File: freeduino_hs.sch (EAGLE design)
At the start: 46 parts, among them J1 DC-005, Q1 16 MHz, Q2 12 MHz, T1 FDN340P, U1 CH340G, U2 LM393D, U3 ATMEGA328P-PU, U4 REG1117, U5 REG1117, X1 MINI-USB-32005-201

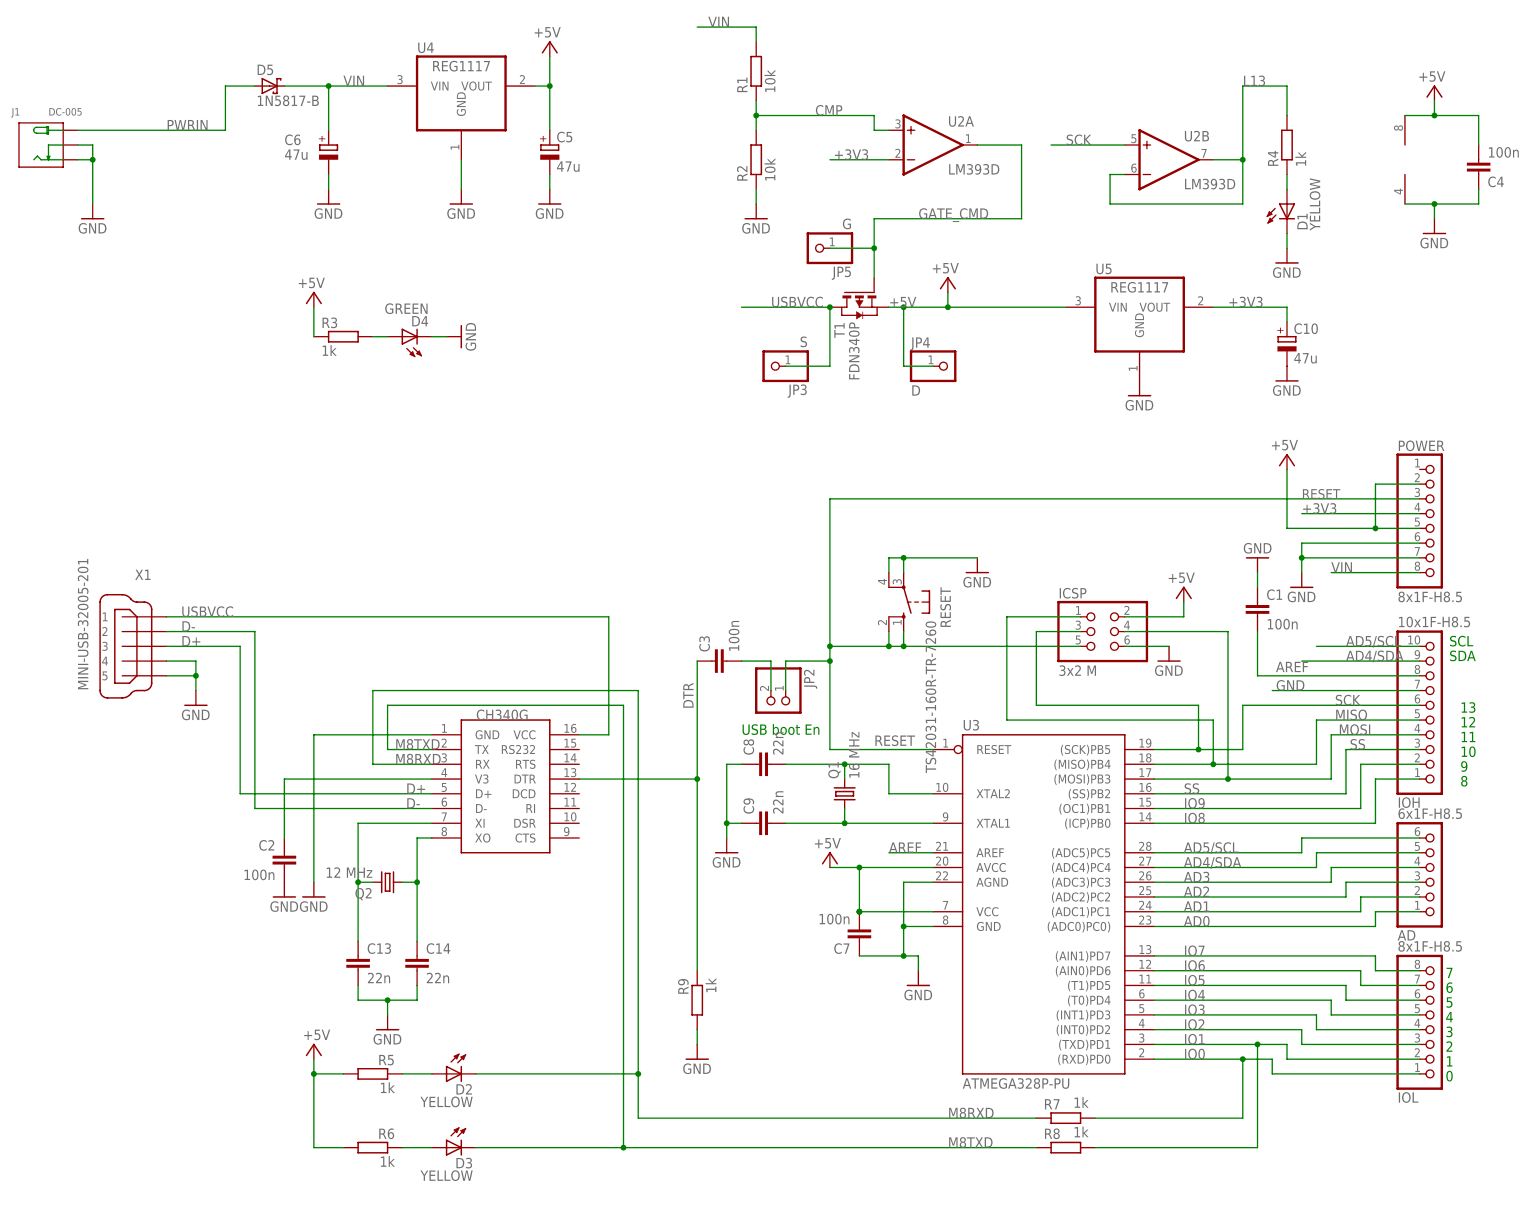
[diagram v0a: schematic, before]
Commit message: Fix TX-RX routing
Move ISP connector
Add reset pull-up resistor
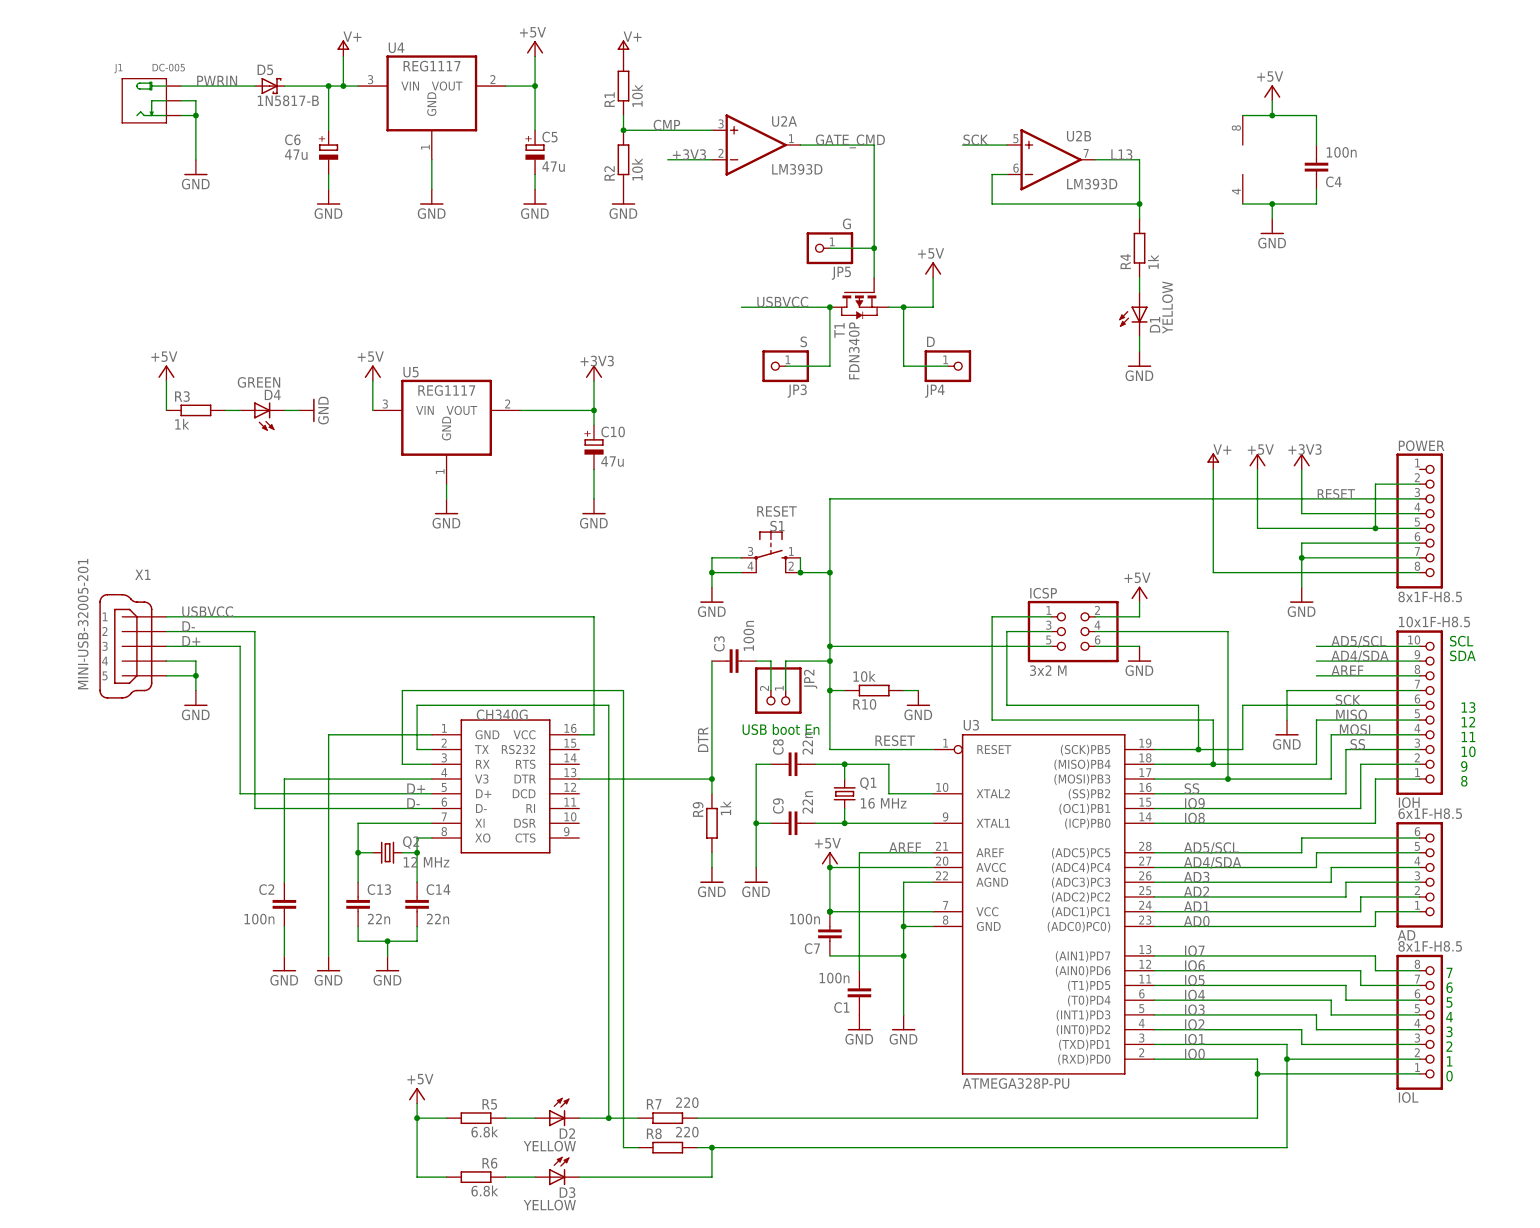
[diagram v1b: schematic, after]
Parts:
- removed RESET: TS42031-160R-TR-7260, switch-omron:10-XX
- added R10: 10k, resistor:R-EU_0204/7
- added S1: RESET, switch-omron:10-XX
- R5, R6: value 1k -> 6.8k
- R7, R8: value 1k -> 220
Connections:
- net VIN renamed V+
- removed net M8TXD: D3.C, R8.1, U1.TX
- new net N$93: D2.C, R7.1, U1.TX
- net GND: now also R10.2, S1.P, S1.P1; no longer RESET.P, RESET.P1
- net IO1: now also D3.C
- net M8RXD: now also R8.1; no longer D2.C, R7.1
- net RESET: now also R10.1, S1.S, S1.S1; no longer RESET.S, RESET.S1
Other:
- moved on the sheet: C1, C10, C13, C14, C2, C3, C4, C5, C7, C8, C9, D1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

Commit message: Re-route some traces
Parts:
- C1, C2, C3, C4, C7: device SmartPrj:C-EU050-024X044 -> rcl_edited:C-EU050-024X044
- C13, C14, C8, C9: device rcl:C-EU050-024X044 -> rcl_edited:C-EU050-024X044
- J1: device Seeed-OPL-Connector:CONN-POWER-JACK-2.1MM(DC-005) -> OPL_Connector:CONN-POWER-JACK-2.1MM(DC-005)
- U2: value LM393D -> LM358

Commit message: Fix reset pull-up
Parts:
- U2: value LM358 -> LMV358; device linear:LM393D -> linear:LMV358M
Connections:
- net +5V: now also R10.2
- net GND: no longer R10.2
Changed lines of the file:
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@@
 <part name="S1" library="switch-omron" library_urn="urn:adsk.eagle:library:377" deviceset="10-XX" device="" package3d_urn="urn:adsk.eagle:package:27496/1" value="RESET"/>
 <part name="POWER" library="SmartPrj" deviceset="PINHD-1X8" device="" value="8x1F-H8.5"/>
-<part name="U2" library="linear" library_urn="urn:adsk.eagle:library:262" deviceset="LM393" device="D" package3d_urn="urn:adsk.eagle:package:16404/2" value="LM358"/>
+<part name="U2" library="linear" library_urn="urn:adsk.eagle:library:262" deviceset="LMV358?*" device="M" package3d_urn="urn:adsk.eagle:package:16404/2" value="LMV358"/>
 <part name="U4" library="burr-brown" library_urn="urn:adsk.eagle:library:111" deviceset="REG1117" device="" package3d_urn="urn:adsk.eagle:package:4940/1"/>
 <part name="U5" library="burr-brown" library_urn="urn:adsk.eagle:library:111" deviceset="REG1117" device="" package3d_urn="urn:adsk.eagle:package:4940/1"/>
@@
 <part name="J1" library="OPL_Connector" deviceset="CONN-POWER-JACK-2.1MM(DC-005)" device="" package3d_urn="urn:adsk.eagle:package:8004506/1" value="DC-005"/>
 <part name="R10" library="resistor" library_urn="urn:adsk.eagle:library:348" deviceset="R-EU_" device="0204/7" package3d_urn="urn:adsk.eagle:package:23498/2" value="10k"/>
-<part name="GND7" library="supply1" library_urn="urn:adsk.eagle:library:371" deviceset="GND" device=""/>
 <part name="P+2" library="supply1" library_urn="urn:adsk.eagle:library:371" deviceset="+5V" device=""/>
 <part name="+3V1" library="supply1" library_urn="urn:adsk.eagle:library:371" deviceset="+3V3" device=""/>
@@
 <part name="P+11" library="supply1" library_urn="urn:adsk.eagle:library:371" deviceset="V+" device="" value="V+"/>
 <part name="P+12" library="supply1" library_urn="urn:adsk.eagle:library:371" deviceset="V+" device="" value="V+"/>
+<part name="P+13" library="supply1" library_urn="urn:adsk.eagle:library:371" deviceset="+5V" device=""/>
 </parts>
 <sheets>
@@
 <attribute name="VALUE" x="123.19" y="92.202" size="1.778" layer="96" rot="MR180"/>
 </instance>
-<instance part="GND7" gate="1" x="134.62" y="86.36" smashed="yes">
-<attribute name="VALUE" x="132.08" y="83.82" size="1.778" layer="96"/>
-</instance>
 <instance part="P+2" gate="1" x="40.64" y="144.78" smashed="yes">
 <attribute name="VALUE" x="42.545" y="147.32" size="1.778" layer="96" rot="R180"/>
@@
 <instance part="P+12" gate="1" x="83.82" y="200.66" smashed="yes">
 <attribute name="VALUE" x="83.82" y="200.66" size="1.778" layer="96"/>
+</instance>
+<instance part="P+13" gate="1" x="134.62" y="91.44" smashed="yes">
+<attribute name="VALUE" x="132.715" y="91.44" size="1.778" layer="96"/>
 </instance>
 </instances>
@@
 <pinref part="P+2" gate="1" pin="+5V"/>
 <wire x1="40.64" y1="137.16" x2="40.64" y2="142.24" width="0.1524" layer="91"/>
+</segment>
+<segment>
+<pinref part="R10" gate="G$1" pin="2"/>
+<wire x1="132.08" y1="88.9" x2="134.62" y2="88.9" width="0.1524" layer="91"/>
+<pinref part="P+13" gate="1" pin="+5V"/>
 </segment>
 </net>
@@
 </segment>
 <segment>
-<pinref part="R10" gate="G$1" pin="2"/>
-<pinref part="GND7" gate="1" pin="GND"/>
-<wire x1="132.08" y1="88.9" x2="134.62" y2="88.9" width="0.1524" layer="91"/>
-</segment>
-<segment>
